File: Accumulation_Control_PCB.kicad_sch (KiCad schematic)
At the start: 241 parts

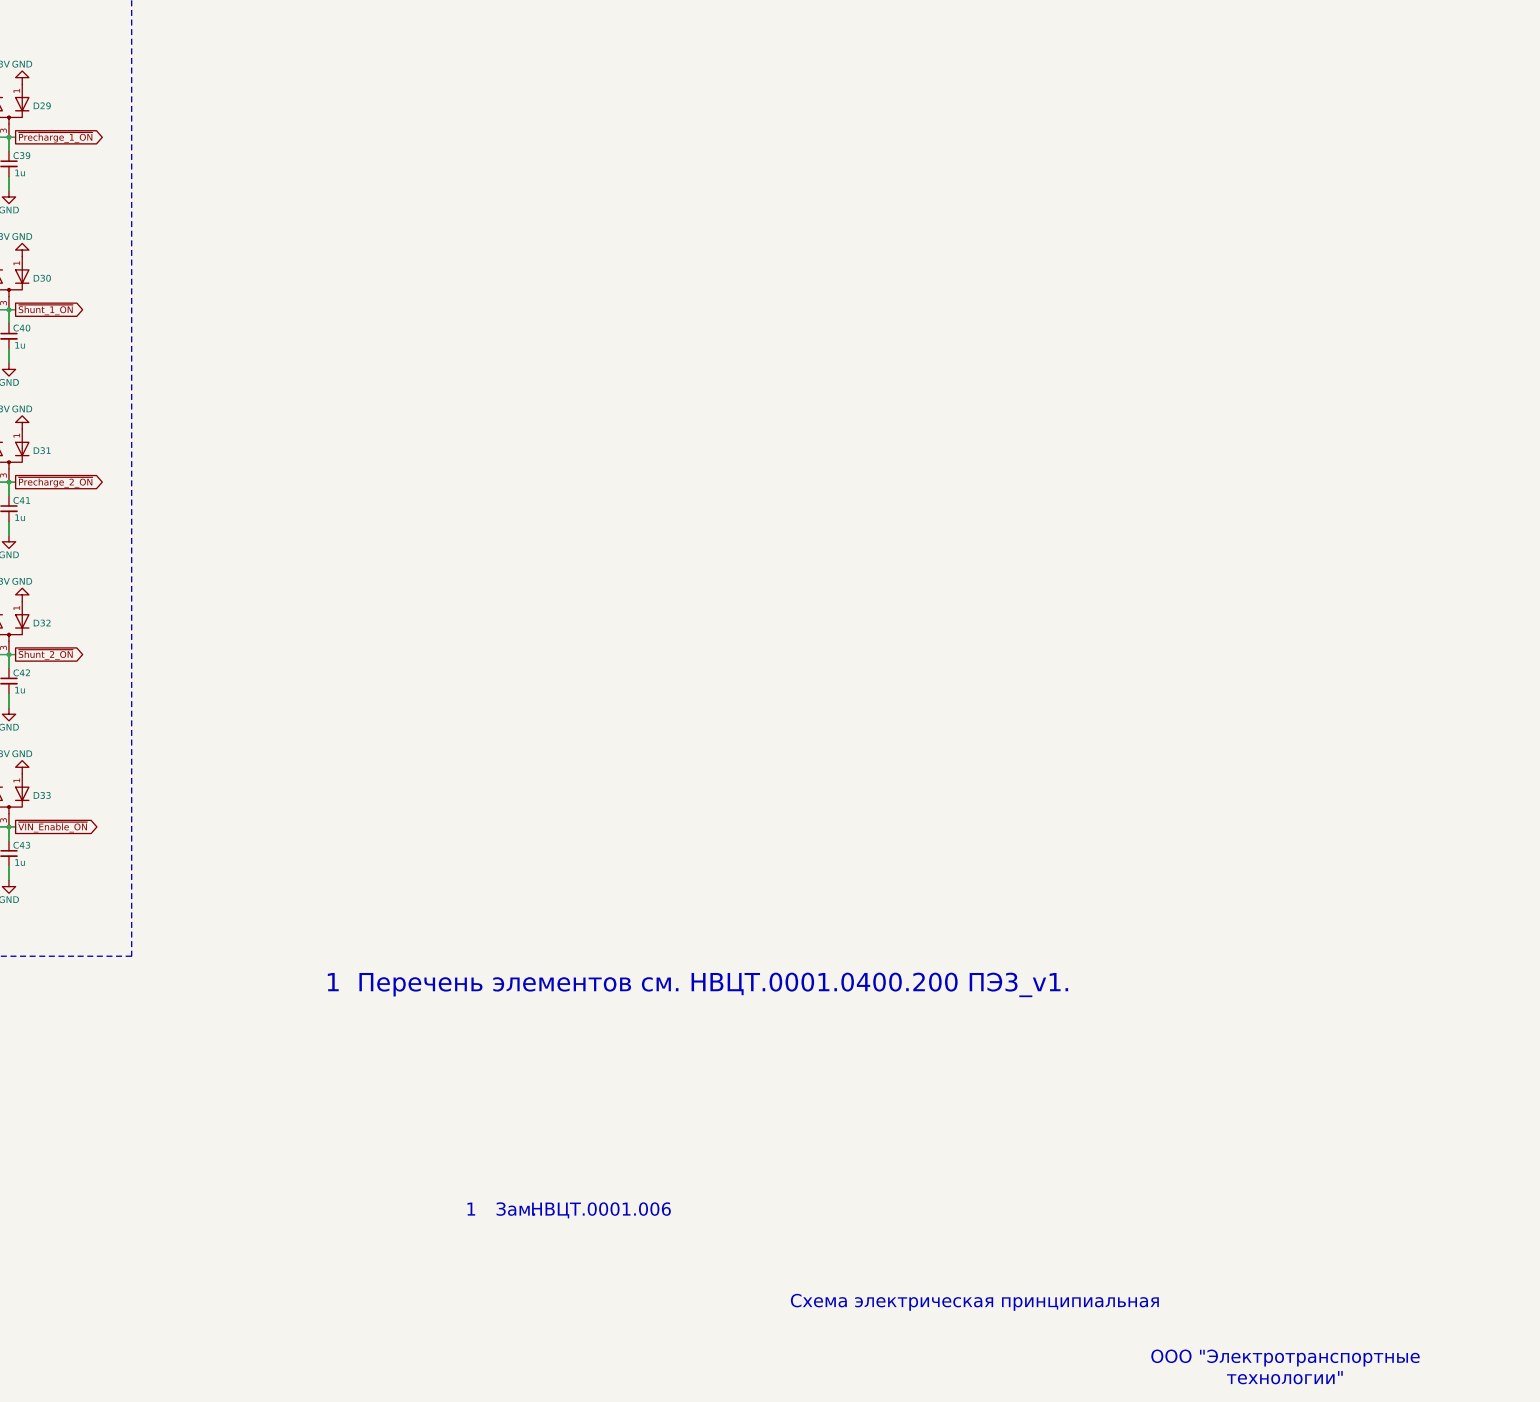
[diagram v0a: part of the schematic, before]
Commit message: VER1.0: добавил один канал управления клапаном
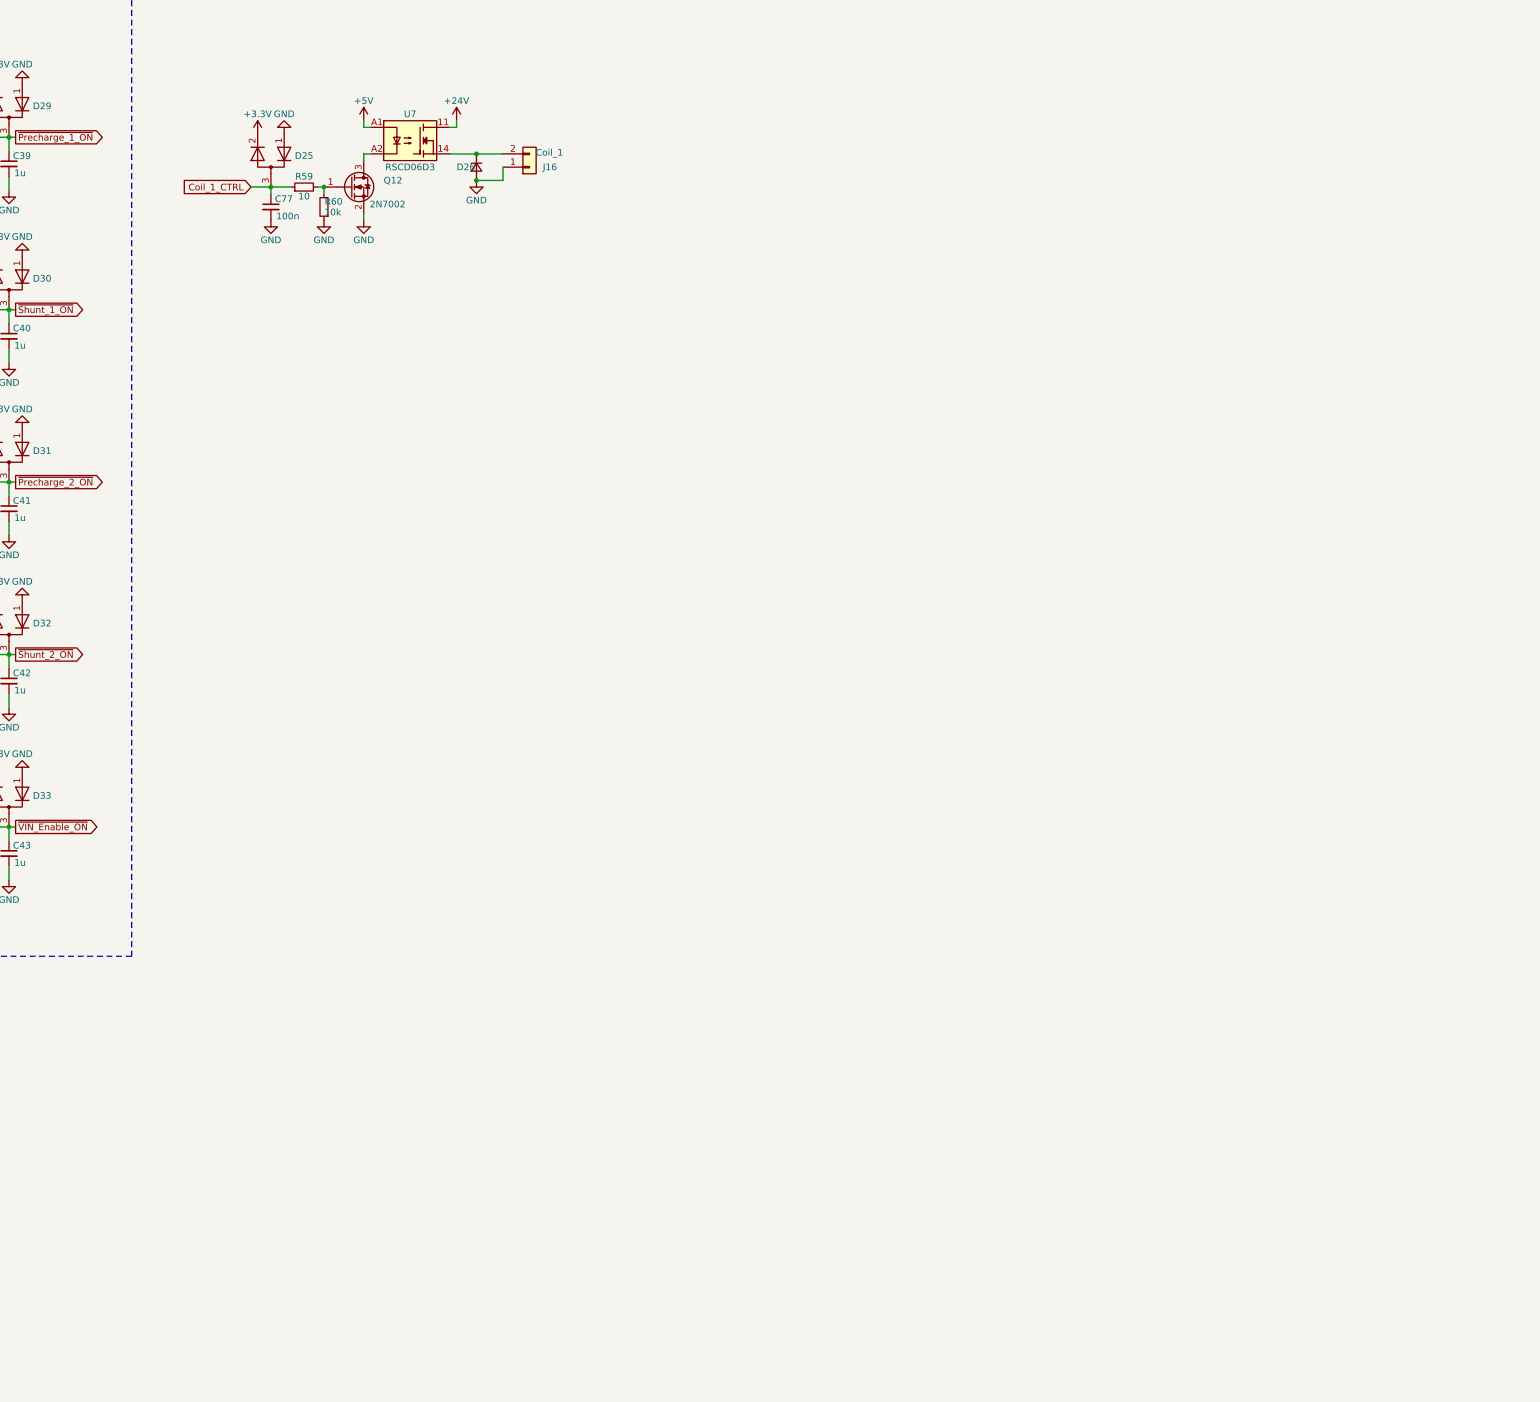
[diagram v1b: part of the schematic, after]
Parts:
- added C77: 100n, Capacitor_SMD:C_0805_2012Metric_Pad1.18x1.45mm_HandSolder, symbol Device:C_Small
- added D25: ~, Package_TO_SOT_SMD:SOT-23, symbol Device:D_Dual_Series_AKC_Parallel
- added D26: ~, Diode_SMD:D_SMA_Handsoldering, symbol Device:D_Small
- added J16: ~, Connector_My:Mini-Fit_01x02_Vertical, symbol Connector_Generic:Conn_01x02
- added Q12: ~, Package_TO_SOT_SMD:SOT-23, symbol Transistor_FET:2N7002
- added R59: 10, Resistor_SMD:R_0805_2012Metric_Pad1.20x1.40mm_HandSolder, symbol Device:R_Small
- added R60: 10k, Resistor_SMD:R_0805_2012Metric_Pad1.20x1.40mm_HandSolder, symbol Device:R_Small
- added U7: RSCD06D3, OptoDevice:Finder_34.81, symbol Relay_SolidState:34.81-7048
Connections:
- net +24V: now also U7.11
- net +3.3V: now also D25.2 (K)
- net +5V: now also U7.A1
- net GND: now also C77.2, D25.1 (A), D26.2 (A), J16.1 (Pin_1), Q12.2 (S), R60.1
- new net: D26.1 (K), J16.2 (Pin_2), U7.14
- new net: Q12.3 (D), U7.A2
- new net: Q12.1 (G), R59.2, R60.2
- new net Coil_1_CTRL: C77.1, D25.3 (common), R59.1
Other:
- note removed: "1"
- note removed: "1 Перечень элементов см. НВЦТ.0001.0400.200 ПЭ3_v1."
- note removed: "Зам."
- note removed: "НВЦТ.0001.006"
- note removed: "ООО "Электротранспортные"
- note removed: "Схема электрическая принципиальная"
- note removed: "технологии""

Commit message: VER1.0: размножил на 8 каналов всего, отвязал 24Въ
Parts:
- removed D13: ~, Diode_SMD:D_SMA_Handsoldering, symbol Device:D_Small
- removed D14, D21, D23: ~, LED_SMD:LED_0805_2012Metric, symbol Device:LED_Small
- removed D30, D32, D33: ~, Package_TO_SOT_SMD:SOT-23, symbol Device:D_Dual_Series_AKC_Parallel
- removed J14: ~, Connector_PinHeader_2.54mm:PinHeader_2x04_P2.54mm_Vertical, symbol Connector_Generic:Conn_01x08
- removed Q10, Q6, Q7, Q8, Q9: ~, Package_TO_SOT_SMD:SOT-23, symbol Transistor_FET:2N7002
- added C78, C79, C80, C82, C83, C84: 100n, Capacitor_SMD:C_0805_2012Metric_Pad1.18x1.45mm_HandSolder, symbol Device:C_Small
- added C81, C85, C86, C87, C88: 1u, Capacitor_SMD:C_0805_2012Metric_Pad1.18x1.45mm_HandSolder, symbol Device:C_Small
- added D13: BZX84C5V1, Package_TO_SOT_SMD:SOT-23_Handsoldering, symbol Device:D_Zener_Small
- added D14, D33, D47, D50, D53, D55, D57, D61, D64, D67, D70: ~, Diode_SMD:D_SMA_Handsoldering, symbol Device:D_Small
- added D21, D23, D45, D48, D51, D59, D62, D65, D68, D71, D73, D75, D77: ~, Package_TO_SOT_SMD:SOT-23, symbol Device:D_Dual_Series_AKC_Parallel
- added D27, D30, D32, D46, D49, D52, D54, D56, D58, D60, D63, D66, D69, D72, D74, D76, D78: ~, LED_SMD:LED_0805_2012Metric, symbol Device:LED_Small
- added J17, J18, J19, J23, J24, J25, J26, J27, J28, J29, J30, J31, J32: ~, Connector_My:Mini-Fit_01x02_Vertical, symbol Connector_Generic:Conn_01x02
- added Q10, Q16, Q17: ~, Package_TO_SOT_SMD:SOT-223, symbol Driver_FET:BSP75N
- added Q13, Q14, Q15, Q18, Q19, Q20, Q21: ~, Package_TO_SOT_SMD:SOT-23, symbol Transistor_FET:2N7002
- added R100, R104, R107, R94, R96, R98: 330, Resistor_SMD:R_0805_2012Metric_Pad1.20x1.40mm_HandSolder, symbol Device:R_Small
- added R101, R103, R106, R109, R112, R115, R118, R121, R123, R126, R129, R63, R83, R93, R97, R99: 10k, Resistor_SMD:R_0805_2012Metric_Pad1.20x1.40mm_HandSolder, symbol Device:R_Small
- added R102, R105, R108, R111, R114, R117, R120, R125, R128, R58, R62, R82, R92: 8.2k, Resistor_SMD:R_0805_2012Metric_Pad1.20x1.40mm_HandSolder, symbol Device:R_Small
- added R110, R113, R116, R119, R61, R81, R91: 1k, Resistor_SMD:R_0805_2012Metric_Pad1.20x1.40mm_HandSolder, symbol Device:R_Small
- added R122, R124, R127: 3.3k, Resistor_SMD:R_0805_2012Metric_Pad1.20x1.40mm_HandSolder, symbol Device:R_Small
- added R95: 2.4k, Resistor_SMD:R_1206_3216Metric_Pad1.30x1.75mm_HandSolder, symbol Device:R_Small
- added U10, U20, U21, U22, U23, U8, U9: RSCD06D3, OptoDevice:Finder_34.81, symbol Relay_SolidState:34.81-7048
- added U11, U12, U13, U14, U15, U16, U17, U18, U19, U24, U25, U26, U27, U28, U29, U30: PC817, Package_DIP:DIP-4_W7.62mm, symbol Isolator:PC817
- C43: value 1u -> 100n
- D20: Description P/N Yellow LED -> Blue LED; Product Name FYLS-0805UYC -> FYLS-0805UBC
- J10: Purpose Precharge 2 -> Relay_3
- J11: Purpose Shunt 2 -> Relay_4
- J12: Purpose VIN Enable -> Shunt 1
- J7: Purpose VIN Enable -> Precharge 1
- J8: Purpose Precharge 1 -> Relay_1
- J9: Purpose Shunt 1 -> Relay_2
- R12, R77: value 8.2k -> 10k
- R40, R65, R71: value 10k -> 3.3k
- R41, R69, R73: value 10k -> 8.2k
- R43: value 10k -> 330
- R59: value 10 -> 1k
- R66, R72: value 100 -> 8.2k
- R68: value 100 -> 3.3k
- R70, R74: value 100 -> 10k
- R76: value 8.2k -> 330
- R78: value 8.2k -> 3.3k
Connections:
- net +24V: now also D20.2 (A), D14.1 (K), D54.2 (A), D55.1 (K), D56.2 (A), D57.1 (K), D58.2 (A), J23.2 (Pin_2), J24.2 (Pin_2), J29.2 (Pin_2), J30.2 (Pin_2), J31.2 (Pin_2), J32.2 (Pin_2), R95.2, U10.11, U20.11, U21.11, U22.11, U23.11, U8.11, U9.11; no longer D6.1 (K), J12.2 (Pin_2), J2.2 (Pin_2)
- net +3.3V: now also D21.2 (K), D23.2 (K), D45.2 (K), D48.2 (K), D51.2 (K), D59.2 (K), D62.2 (K), D65.2 (K), D68.2 (K), D71.2 (K), D73.2 (K), D75.2 (K), D77.2 (K), U19.4, U24.4, U25.4, U26.4, U27.4, U28.4, U29.4, U30.4; no longer R66.2, R68.2, R70.2, R72.2, R74.2
- net +5V: now also U10.A1, U20.A1, U21.A1, U22.A1, U23.A1, U8.A1, U9.A1
- net GND: now also R1.2, R67.2, R70.2, C78.2, C79.2, C80.2, C82.2, C83.2, C84.2, C85.2, C86.2, C87.2, C88.2, D21.1 (A), D23.1 (A), D45.1 (A), D48.1 (A), D51.1 (A), D59.1 (A), D62.1 (A), D65.1 (A), D68.1 (A), D71.1 (A), D73.1 (A), D75.1 (A), D77.1 (A), Q13.2 (S), Q14.2 (S), Q15.2 (S), Q18.2 (S), Q19.2 (S), Q20.2 (S), Q21.2 (S), R112.1, R115.1, R118.1, R121.1, R123.2, R126.2, R129.2, R63.1, R83.1, R93.1, U11.2, U12.2, U13.2, U14.2, U15.2, U16.2, U17.2, U18.2; no longer D26.2 (A), J16.1 (Pin_1), Q1.3 (S), Q1.4 (S), Q2.3 (S), Q2.4 (S), Q3.3 (S), Q3.4 (S), Q4.3 (S), Q4.4 (S), Q5.3 (S), Q5.4 (S), R1.1, R40.1, R41.1, R43.1, R76.2, R78.2, R79.2, R80.2
- net GNDPWR: now also D26.2 (A), J16.1 (Pin_1), Q1.3 (S), Q1.4 (S), Q2.3 (S), Q2.4 (S), Q3.3 (S), Q3.4 (S), Q4.3 (S), Q4.4 (S), Q5.3 (S), Q5.4 (S), R12.1, R41.2, R66.2, R69.2, R72.2, R74.1, R79.2, R80.2, C81.2, D13.2 (A), D47.2 (A), D50.2 (A), D53.2 (A), D61.2 (A), D64.2 (A), D67.2 (A), D70.2 (A), J17.1 (Pin_1), J18.1 (Pin_1), J19.1 (Pin_1), J25.1 (Pin_1), J26.1 (Pin_1), J27.1 (Pin_1), J28.1 (Pin_1), Q10.3 (S), Q10.4 (S), Q16.3 (S), Q16.4 (S), Q17.3 (S), Q17.4 (S), R101.1, R103.1, R106.1, R109.1, R111.2, R114.2, R117.2, R120.2, R125.2, R128.2, R58.2, R62.2, R82.2, R92.2, R97.1, R99.1, U19.2, U24.2, U25.2, U26.2, U27.2, U28.2, U29.2, U30.2
- net Precharge_1: no longer Q1.1 (G)
- net Precharge_2: no longer Q3.1 (G)
- net Shunt_1: no longer Q2.1 (G)
- net Shunt_2: no longer Q4.1 (G)
- net VIN_Enable: no longer Q5.1 (G)
- net ~{Precharge_1_ON}: no longer C39.1, D29.3 (common), R66.1
- net ~{Precharge_2_ON}: no longer C41.1, D31.3 (common), R70.1
- net ~{Shunt_1_ON}: no longer C40.1, R68.1
- net ~{Shunt_2_ON}: no longer C42.1, R72.1
- net ~{VIN_Enable_ON}: no longer C43.1, R74.1
- net at D26.1 (K), J16.2 (Pin_2), U7.14: now also D27.2 (A)
- net Relay_5_ON: now reaches R77.1
- net Relay_5_ON: now also C85.1, D71.3 (common), U27.3
- net at R40.2: now also D22.2 (A), J9.1 (Pin_1); no longer R67.2
- net at J7.1 (Pin_1), Q5.2 (D): now also R73.2, D14.2 (A); no longer R12.2
- net at R43.2: now also U15.1; no longer R73.2
- net at R78.1: now also U28.1; no longer D22.1 (K)
- net at D20.1 (K): now also R73.1; no longer R76.1
- net at R71.2: now also D72.2 (A), J29.1 (Pin_1); no longer R42.1
- net Relay_3_ON: now reaches R67.1
- net Relay_3_ON: now also C41.1, D23.3 (common), U25.3; no longer J9.1 (Pin_1)
- net at R79.1: now also D74.1 (K)
- net at D24.2 (A), J8.1 (Pin_1): now also R122.2; no longer R65.1
- net at R65.2: now also J10.1 (Pin_1), D30.2 (A); no longer R1.2
- net at J11.1 (Pin_1): now also R68.2, D32.2 (A); no longer R71.1
- new net: Q21.1 (G), R119.2, R121.2
- new net: R127.1, U30.1
- new net: Q13.1 (G), R61.2, R63.2
- new net: D66.1 (K), R117.1
- new net: D52.1 (K), R92.1
- new net: D55.2 (A), J23.1 (Pin_1), Q16.2 (D), R105.2
- new net: Q4.1 (G), R101.2, U14.3
- new net: D57.2 (A), J24.1 (Pin_1), Q17.2 (D), R108.2
- new net: R65.1, U25.1
- new net: Q15.1 (G), R91.2, R93.2
- new net: D32.1 (K), R69.1
- new net: D33.1 (K), J12.2 (Pin_2)
- new net: D33.2 (A), J12.1 (Pin_1), Q10.2 (D), R102.2
- new net: D78.1 (K), R128.1
- new net: D78.2 (A), J32.1 (Pin_1), R127.2
- new net: Q3.1 (G), R99.2, U13.3
- new net: R40.1, U24.1
- new net: Q21.3 (D), U23.A2
- new net: D63.2 (A), D64.1 (K), J26.2 (Pin_2), U21.14
- new net: Q19.3 (D), U21.A2
- new net: R94.2, U11.1
- new net: Q1.1 (G), R12.2, U11.3
- new net: D66.2 (A), D67.1 (K), J27.2 (Pin_2), U22.14
- new net: Q14.1 (G), R81.2, R83.2
- new net: D46.2 (A), D47.1 (K), J17.2 (Pin_2), U8.14
- new net: D49.1 (K), R82.1
- new net: D49.2 (A), D50.1 (K), J18.2 (Pin_2), U9.14
- new net: D69.2 (A), D70.1 (K), J28.2 (Pin_2), U23.14
- new net: D69.1 (K), R120.1
- new net: D63.1 (K), R114.1
- new net: Q18.1 (G), R110.2, R112.2
- new net: D27.1 (K), R58.1
- new net: R122.1, U19.1
- new net: Q5.1 (G), R74.2, U15.3
- new net: R76.2, U16.1
- new net: Q10.1 (G), R103.2, U16.3
- new net: D54.1 (K), R102.1
- new net: R96.2, U12.1
- new net: D30.1 (K), R66.1
- new net: Q2.1 (G), R97.2, U12.3
- new net: Q16.1 (G), R106.2, U17.3
- new net: D52.2 (A), D53.1 (K), J19.2 (Pin_2), U10.14
- new net: D22.1 (K), R41.1
- new net: D76.2 (A), J31.1 (Pin_1), R124.2
- new net: R104.2, U17.1
- new net: Q17.1 (G), R109.2, U18.3
- new net: R100.2, U14.1
- new net: D6.1 (K), J2.2 (Pin_2)
- new net: Q13.3 (D), U8.A2
- new net: Q20.1 (G), R116.2, R118.2
- new net: Q18.3 (D), U20.A2
- new net: R71.1, U27.1
- new net: D74.2 (A), J30.1 (Pin_1), R78.2
- new net: R68.1, U26.1
- new net: D60.2 (A), D61.1 (K), J25.2 (Pin_2), U20.14
- new net: D56.1 (K), R105.1
- new net: D60.1 (K), R111.1
- new net: R98.2, U13.1
- new net: Q14.3 (D), U9.A2
- new net: D72.1 (K), R72.1
- new net: Q19.1 (G), R113.2, R115.2
- new net: Q20.3 (D), U22.A2
- new net: R124.1, U29.1
- new net: R107.2, U18.1
- new net: D76.1 (K), R125.1
- new net: D58.1 (K), R108.1
- new net: Q15.3 (D), U10.A2
- new net: D46.1 (K), R62.1
- new net +5.1V: C81.1, D13.1 (K), R95.1, U11.4, U12.4, U13.4, U14.4, U15.4, U16.4, U17.4, U18.4
- new net Coil_2_CTRL: C78.1, D45.3 (common), R61.1
- new net Coil_3_CTRL: C79.1, D48.3 (common), R81.1
- new net Coil_4_CTRL: C80.1, D51.3 (common), R91.1
- new net Coil_5_CTRL: C43.1, D59.3 (common), R110.1
- new net Coil_6_CTRL: C82.1, D62.3 (common), R113.1
- new net Coil_7_CTRL: C83.1, D65.3 (common), R116.1
- new net Coil_8_CTRL: C84.1, D68.3 (common), R119.1
- new net Relay_1: R107.1, R94.1
- new net Relay_1_ON: C39.1, D29.3 (common), R1.1, U19.3
- new net Relay_2: R96.1
- new net Relay_2_ON: C40.1, D21.3 (common), R42.1, U24.3
- new net Relay_3: R98.1
- new net Relay_4: R100.1
- new net Relay_4_ON: C42.1, D31.3 (common), R70.1, U26.3
- new net Relay_5: R43.1
- new net Relay_6: R76.1
- new net Relay_6_ON: C86.1, D73.3 (common), R123.1, U28.3
- new net Relay_7_ON: C87.1, D75.3 (common), R126.1, U29.3
- new net Relay_8: R104.1
- new net Relay_8_ON: C88.1, D77.3 (common), R129.1, U30.3
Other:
- note added: "Управление клапанами"
- moved on the sheet: C39, C77, D10, D11, D12, D24, D25, D26, D29, D4, D6, D7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
